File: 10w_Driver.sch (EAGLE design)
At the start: 24 parts, among them IC1 78L05Z, T4 2N3904, T5 22-23-2021, T6 22-23-2041, T7 2N3904, T8 2N3904, U1 PT4115PT4115B89E, U2 PT4115PT4115B89E, U3 PT4115PT4115B89E

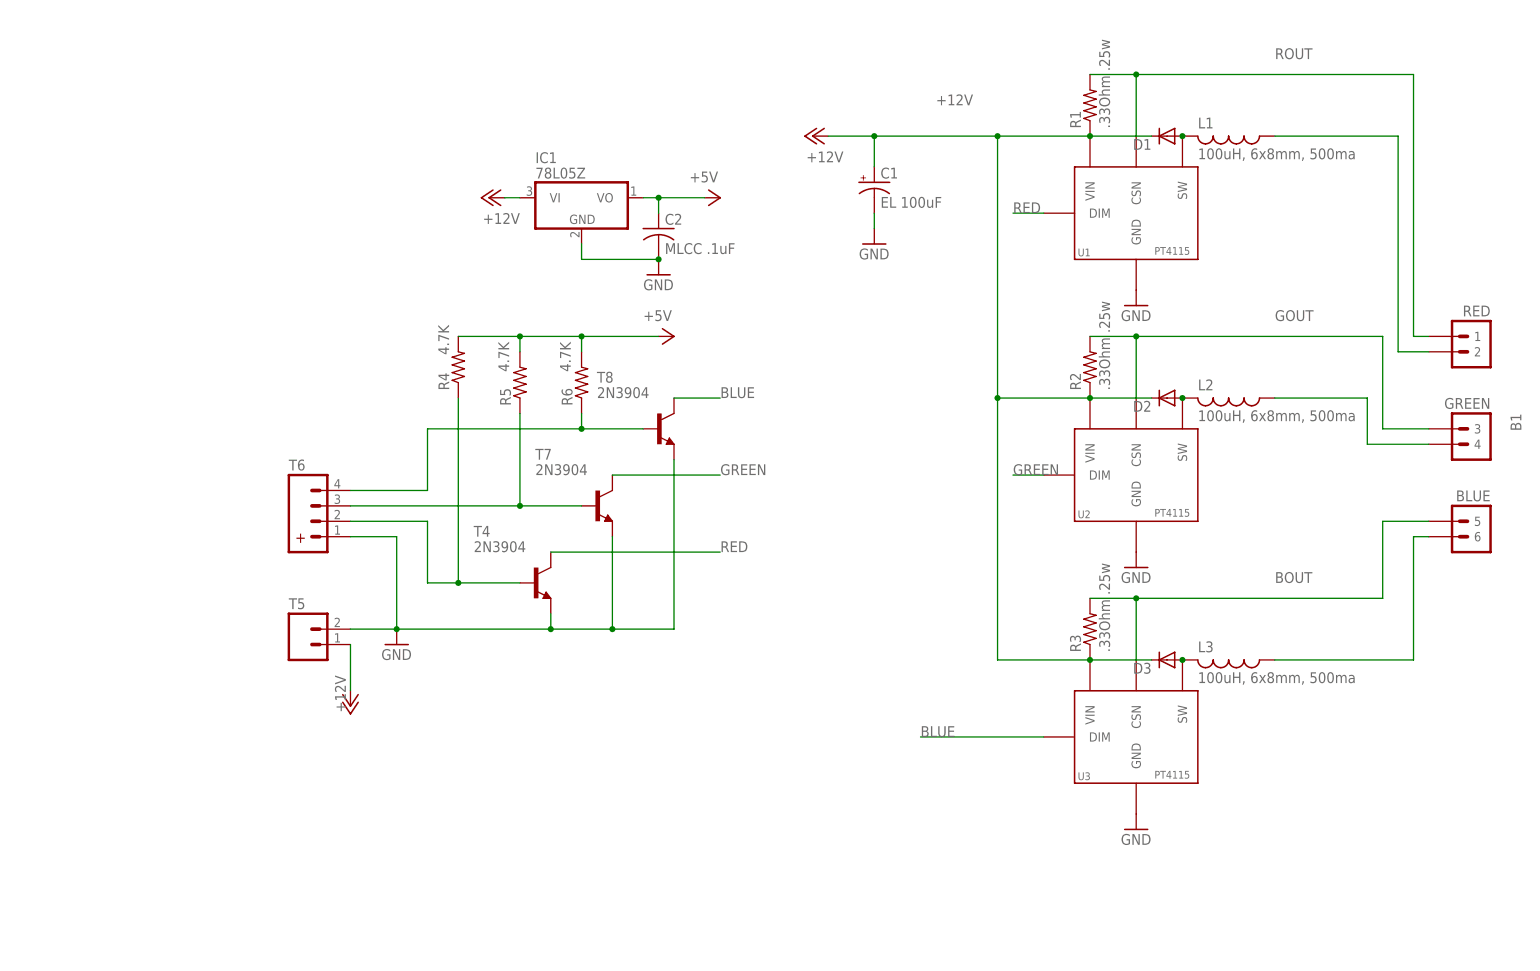
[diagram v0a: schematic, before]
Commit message: Initial Design with ws2811
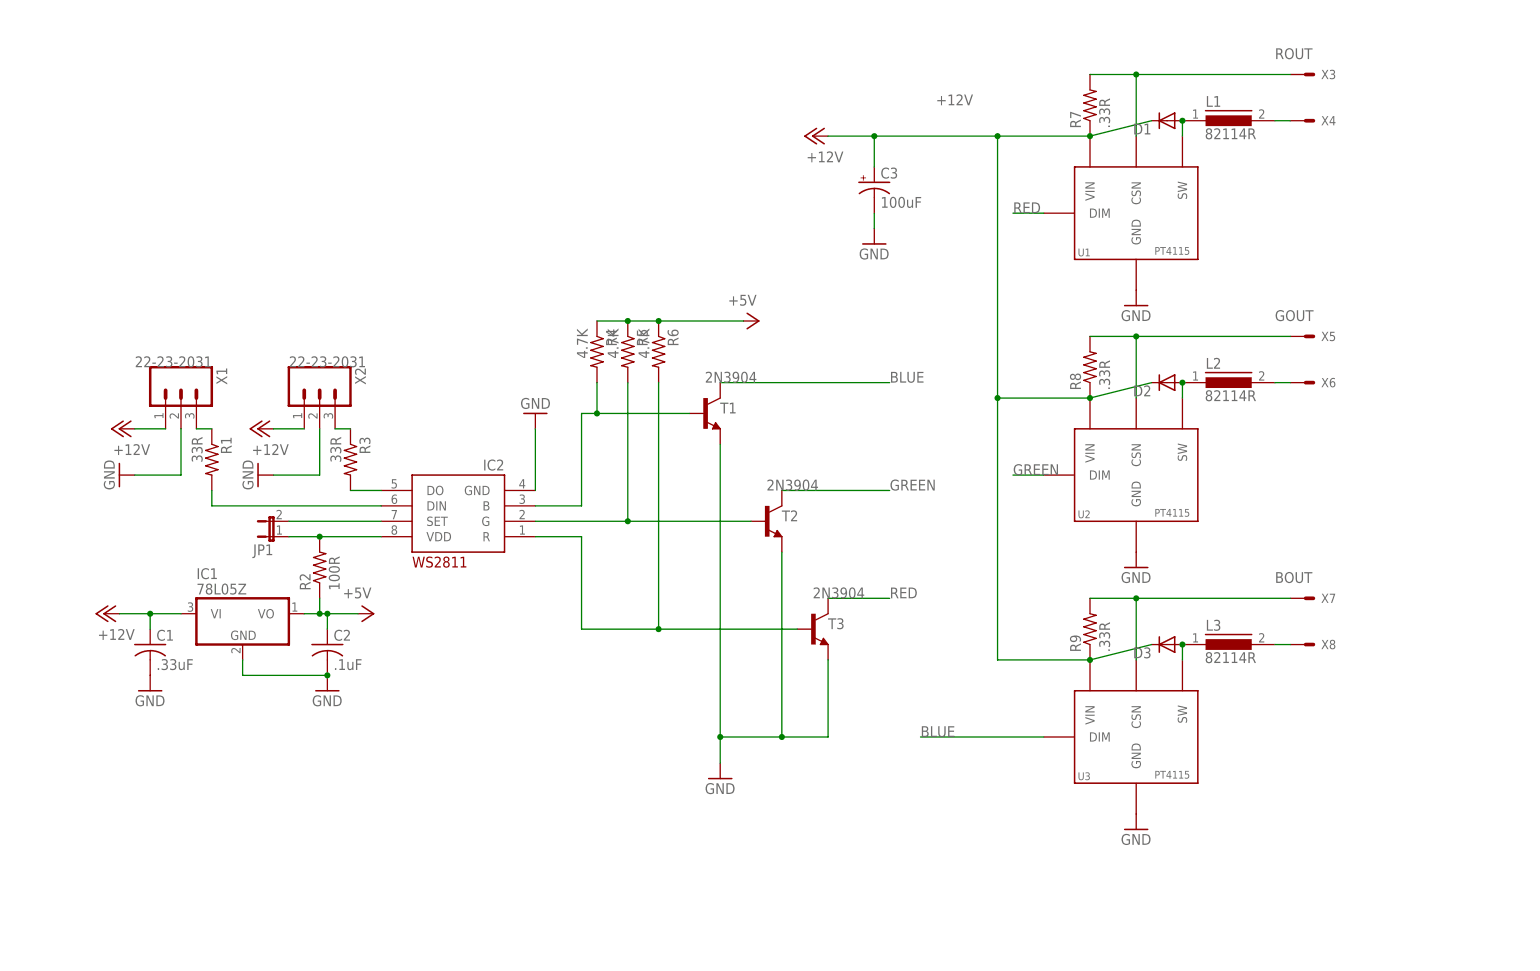
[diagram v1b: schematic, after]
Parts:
- removed B1: LED-BOARD, MyLibrary:LED-BOARD
- removed T4, T7, T8: 2N3904, transistor:2N3904
- removed T5: 22-23-2021, MyLibrary:22-23-2021
- removed T6: 22-23-2041, MyLibrary:22-23-2041
- added C3: 100uF, rcl:CPOL-USTT2D6L
- added IC2: WS2811-SOP8, MyLibrary:WS2811-SOP8
- added JP1: (no value), jumper:JP1E
- added R7, R8, R9: .33R, resistor:R-US_0204/5
- added T1, T2, T3: 2N3904, transistor:2N3904
- added X1, X2: 22-23-2031, MyLibrary:22-23-2031
- added X3, X4, X5, X6, X7, X8: LED-PAD, MyLibrary:LED-PAD
- C1: value EL 100uF -> .33uF; device rcl:CPOL-USTT2D6L -> rcl:C-US025-025X050
- C2: value MLCC .1uF -> .1uF; device rcl:C-US050-030X075 -> rcl:C-US025-025X050
- L1, L2, L3: value 100uH, 6x8mm, 500ma -> 82114R; device MyLibrary:INDUCTOR -> inductors:82114R
- R1, R3: value .33Ohm .25w -> 33R; device resistor:R-US_0204/5 -> rcl:R-US_0204/5
- R2: value .33Ohm .25w -> 100R; device resistor:R-US_0204/5 -> rcl:R-US_0204/5
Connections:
- new net N$16: IC2.SET, JP1.2
- new net N$18: IC2.G, R5.2, T2.B
- new net N$20: IC2.R, R6.2, T3.B
- new net N$7: IC2.DO, R3.2
- new net N$8: IC2.DIN, R1.2
- new net N$9: L2.2, X6.S
- net +12V: now also C1.1, C3.+, R7.1, R8.1, R9.1, X1.1, X2.1; no longer C1.+, R1.1, R2.1, R3.1, T5.1
- net +5V: now also R2.1, R4.1, R5.1, R6.1; no longer R4.2, R5.2, R6.2
- net BLUE: now also T1.C; no longer T8.C
- net BOUT: now also R9.2, X7.S; no longer B1.5, R3.2
- net GND: now also C1.2, C3.-, IC2.GND, T1.E, T2.E, T3.E, X1.2, X2.2; no longer C1.-, T4.E, T5.2, T6.1, T7.E, T8.E
- net GOUT: now also R8.2, X5.S; no longer B1.3, R2.2
- net GREEN: now also T2.C; no longer T7.C
- net N$1: now also L1.1; no longer L1.2
- net N$10: now also L3.2, X8.S; no longer R4.1, T4.B, T6.2
- net N$14: now also IC2.VDD, JP1.1, R2.2; no longer R5.1, T6.3, T7.B
- net N$15: now also IC2.B, R4.2, T1.B; no longer R6.1, T6.4, T8.B
- net N$2: now also L3.1; no longer L3.2
- net N$3: now also L1.2, X4.S; no longer B1.2, L1.1
- net N$4: now also R3.1, X2.3; no longer B1.4, L2.1
- net N$5: now also L2.1; no longer L2.2
- net N$6: now also R1.1, X1.3; no longer B1.6, L3.1
- net RED: now also T3.C; no longer T4.C
- net ROUT: now also R7.2, X3.S; no longer B1.1, R1.2
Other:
- moved on the sheet: C2, D1, D2, D3, IC1, R1, R2, R3, R4, R5, R6

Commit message: Final 1.1
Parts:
- R2: value 100R -> 100ohm
- R4, R5, R6: value 4.7K -> 4.7k
- R7, R8, R9: value .33R -> .33
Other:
- moved on the sheet: C3, D1, D3, L1, L3, R7, R8, U1, U3, X3, X4, X5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

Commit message: Final 1.1 with Inverter
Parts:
- removed C3: 100uF, rcl:CPOL-USTT2D6L
- removed R7, R8, R9: .33, resistor:R-US_0204/5
- removed T1, T2, T3: 2N3904, transistor:2N3904
- added IC3: TC7W04FTC7W04F, MyLibrary:TC7W04FTC7W04F
- added TP1: TPB2,54, testpad:TPB2,54
- added TP2: PTR1TP20SQ, testpad:PTR1TP20SQ
- C1: value .33uF -> EL 100uF; device rcl:C-US025-025X050 -> rcl:CPOL-USTT2D6L
- C2: device rcl:C-US025-025X050 -> resistor:CPOL-USB45181A
- JP1: device jumper:JP1E -> jumper:JP2E
- L1, L2, L3: value 82114R -> SLF7045; device inductors:82114R -> inductors:SLF7045
- R1: value 33R -> .3ohm .25w; device rcl:R-US_0204/5 -> resistor:R-US_R0805
- R2: value 100ohm -> 33R; device rcl:R-US_0204/5 -> rcl:R-US_M0805
- R3: device rcl:R-US_0204/5 -> rcl:R-US_M0805
- R4: value 4.7k -> 100ohm; device resistor:R-US_0204/5 -> rcl:R-US_M0805
- R5: value 4.7k -> .3hm .25w; device resistor:R-US_0204/5 -> resistor:R-US_M0805
- R6: value 4.7k -> .3ohm .25w; device resistor:R-US_0204/5 -> resistor:R-US_R0805
- U1, U2, U3: device MyLibrary:PT4115PT4115B89E -> IC:PT4115PT4115B89E
- X2: value 22-23-2031 -> LED-PAD; device MyLibrary:22-23-2031 -> MyLibrary:LED-PAD
- X4: value LED-PAD -> 22-23-2031; device MyLibrary:LED-PAD -> MyLibrary:22-23-2031
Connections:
- removed net N$20: IC2.R, R6.2, T3.B
- new net N$19: IC2.G, IC3G$3.I
- net +12V: now also C1.+, R1.2, R5.2, R6.2, X4.1; no longer C1.1, C3.+, R7.1, R8.1, R9.1, X2.1
- net +5V: now also C2.+, IC3VCC.S, TP1.TP; no longer C2.1, R2.1, R5.1, R6.1
- net BLUE: now also IC3G$1.O; no longer T1.C
- net BOUT: now also R6.1; no longer R9.2
- net GND: now also C1.-, C2.-, IC3GND.S, TP2.TP, X4.2; no longer C1.2, C2.2, C3.-, T1.E, T2.E, T3.E, X2.2
- net GOUT: now also R5.1; no longer R8.2
- net GREEN: now also IC3G$3.O; no longer T2.C
- net N$14: now also JP1.2, R4.2; no longer JP1.1, R2.2
- net N$15: now also IC2.R, IC3G$2.I; no longer IC2.B, R4.2, T1.B
- net N$16: now also IC2.B, IC3G$1.I; no longer IC2.SET, JP1.2
- net N$18: now also IC2.SET, JP1.3; no longer IC2.G, R5.2, T2.B
- net N$3: now also X3.S; no longer X4.S
- net N$4: now also X4.3; no longer X2.3
- net N$6: now also R2.1; no longer R1.1
- net N$8: now also R2.2; no longer R1.2
- net RED: now also IC3G$2.O; no longer T3.C
- net ROUT: now also R1.1, X2.S; no longer R7.2, X3.S
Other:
- moved on the sheet: D1, D2, D3, IC1, IC2, R1, R2, R3, R4, R5, R6, U1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

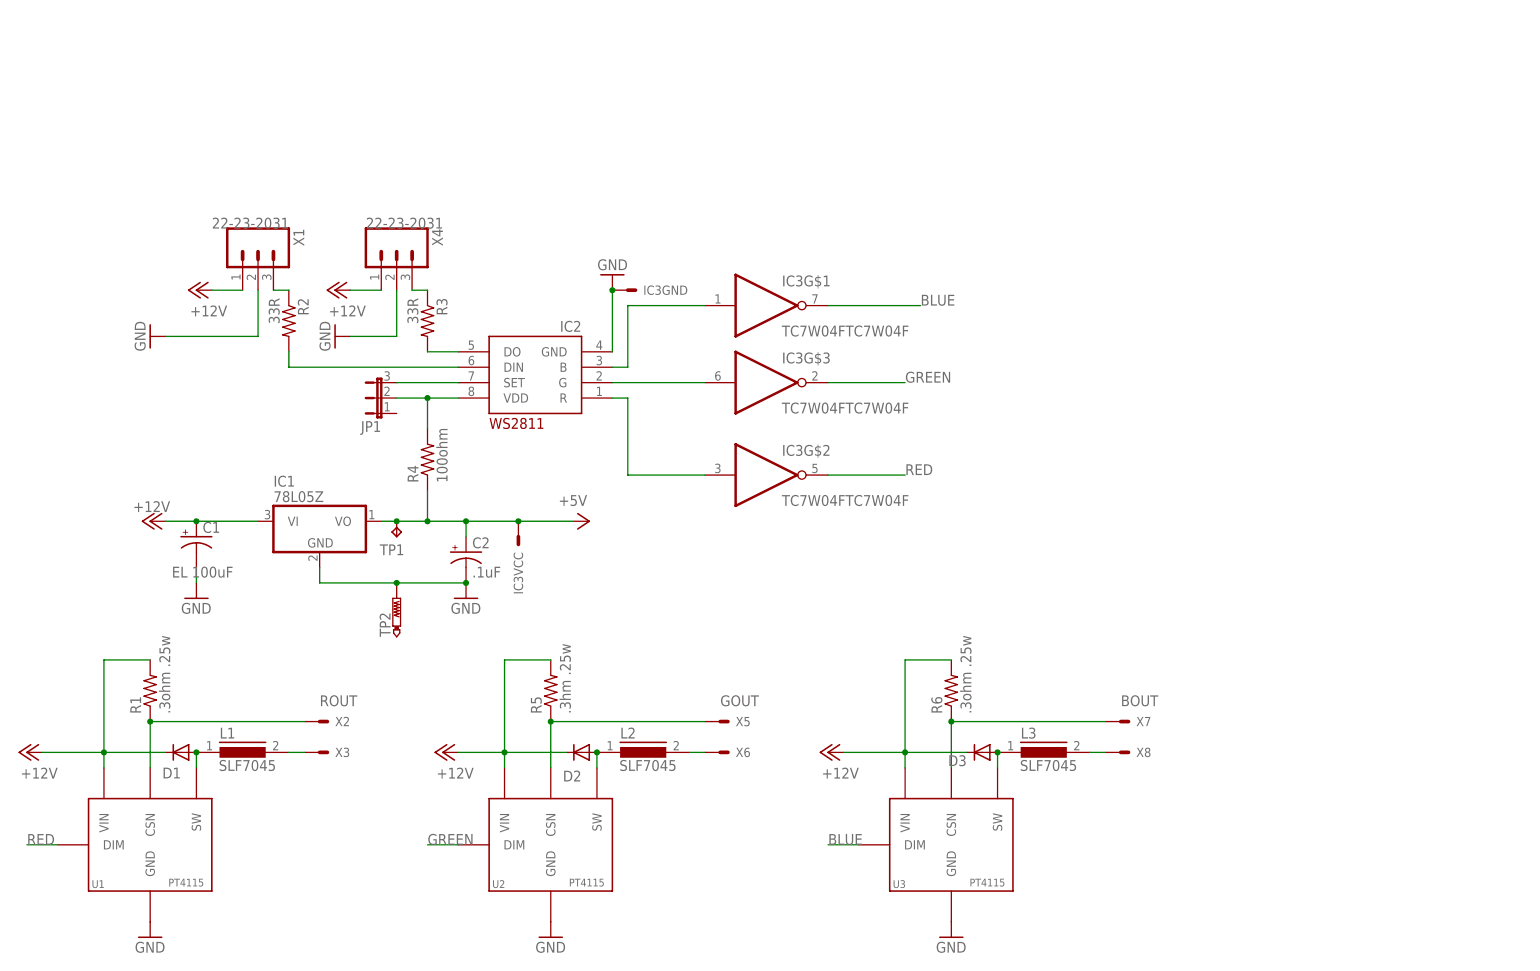
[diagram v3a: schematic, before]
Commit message: Reworked Inverter Layout
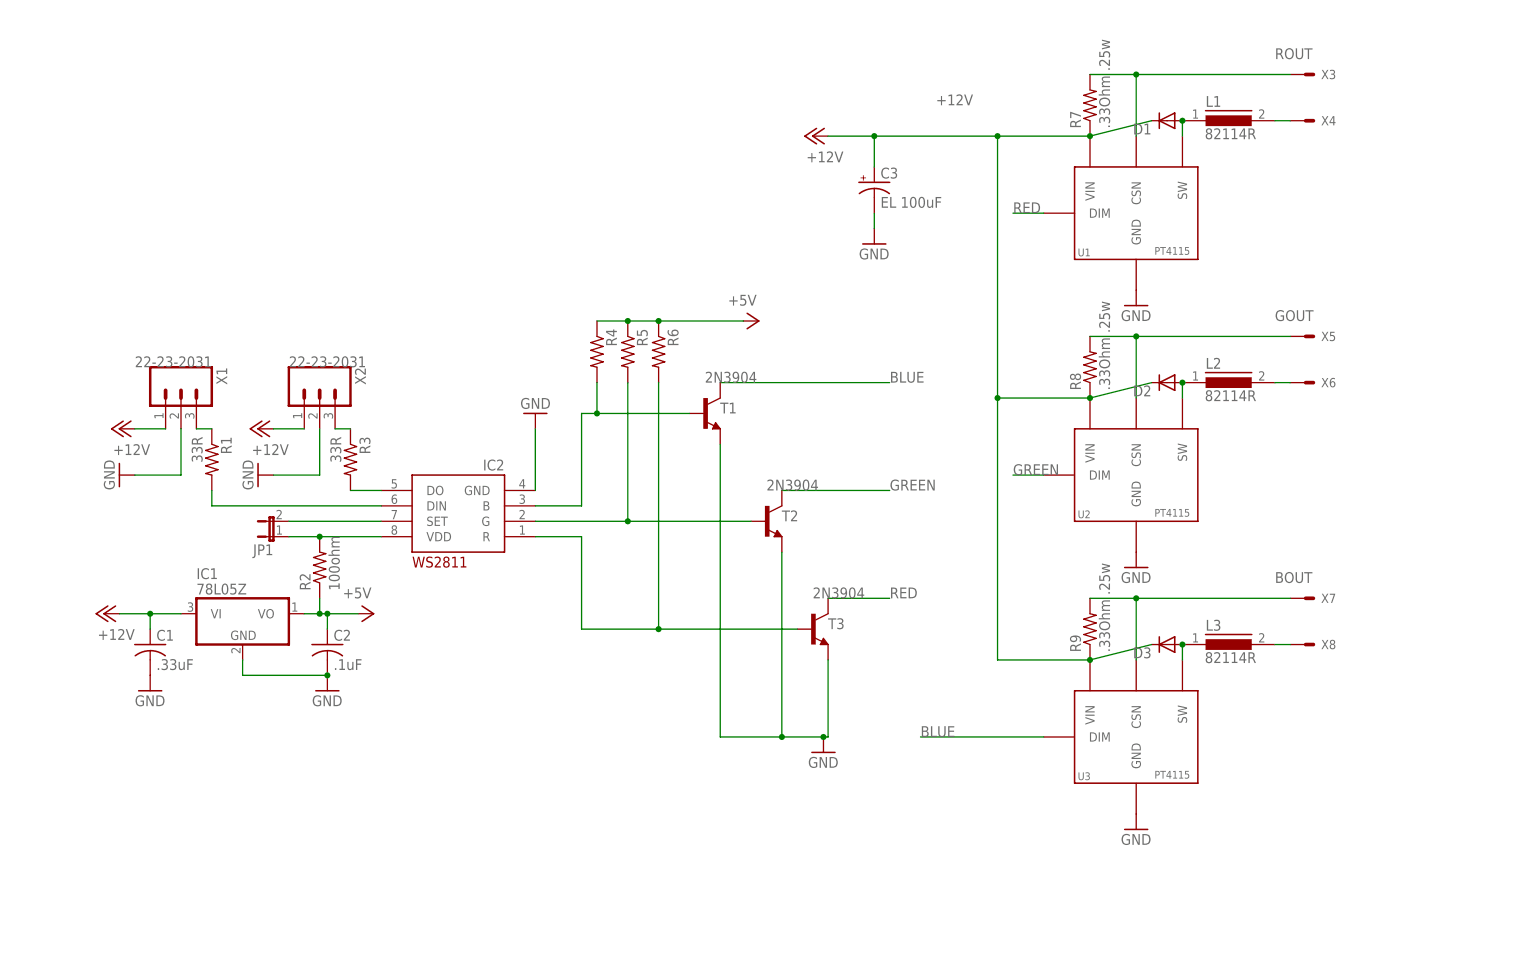
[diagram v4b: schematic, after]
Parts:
- removed IC3: TC7W04FTC7W04F, MyLibrary:TC7W04FTC7W04F
- removed TP1: TPB2,54, testpad:TPB2,54
- removed TP2: PTR1TP20SQ, testpad:PTR1TP20SQ
- added C3: EL 100uF, rcl:CPOL-USTT2D6L
- added R7, R8, R9: .33Ohm .25w, resistor:R-US_0204/5
- added T1, T2, T3: 2N3904, transistor:2N3904
- C1: value EL 100uF -> .33uF; device rcl:CPOL-USTT2D6L -> rcl:C-US025-025X050
- C2: device resistor:CPOL-USB45181A -> rcl:C-US025-025X050
- JP1: device jumper:JP2E -> jumper:JP1E
- L1, L2, L3: value SLF7045 -> 82114R; device inductors:SLF7045 -> inductors:82114R
- R1: value .3ohm .25w -> 33R; device resistor:R-US_R0805 -> rcl:R-US_0204/5
- R2: value 33R -> 100ohm; device rcl:R-US_M0805 -> rcl:R-US_0204/5
- R3: device rcl:R-US_M0805 -> rcl:R-US_0204/5
- R4: value 100ohm -> (none); device rcl:R-US_M0805 -> resistor:R-US_0204/5
- R5: value .3hm .25w -> (none); device resistor:R-US_M0805 -> resistor:R-US_0204/5
- R6: value .3ohm .25w -> (none); device resistor:R-US_R0805 -> resistor:R-US_0204/5
- U1, U2, U3: device IC:PT4115PT4115B89E -> MyLibrary:PT4115PT4115B89E
- X2: value LED-PAD -> 22-23-2031; device MyLibrary:LED-PAD -> MyLibrary:22-23-2031
- X4: value 22-23-2031 -> LED-PAD; device MyLibrary:22-23-2031 -> MyLibrary:LED-PAD
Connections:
- removed net N$19: IC2.G, IC3G$3.I
- new net N$20: IC2.R, R6.2, T3.B
- net +12V: now also C1.1, C3.+, R7.1, R8.1, R9.1, X2.1; no longer C1.+, R1.2, R5.2, R6.2, X4.1
- net +5V: now also C2.1, R2.1, R5.1, R6.1; no longer C2.+, IC3VCC.S, TP1.TP
- net BLUE: now also T1.C; no longer IC3G$1.O
- net BOUT: now also R9.2; no longer R6.1
- net GND: now also C1.2, C2.2, C3.-, T1.E, T2.E, T3.E, X2.2; no longer C1.-, C2.-, IC3GND.S, TP2.TP, X4.2
- net GOUT: now also R8.2; no longer R5.1
- net GREEN: now also T2.C; no longer IC3G$3.O
- net N$14: now also JP1.1, R2.2; no longer JP1.2, R4.2
- net N$15: now also IC2.B, R4.2, T1.B; no longer IC2.R, IC3G$2.I
- net N$16: now also IC2.SET, JP1.2; no longer IC2.B, IC3G$1.I
- net N$18: now also IC2.G, R5.2, T2.B; no longer IC2.SET, JP1.3
- net N$3: now also X4.S; no longer X3.S
- net N$4: now also X2.3; no longer X4.3
- net N$6: now also R1.1; no longer R2.1
- net N$8: now also R1.2; no longer R2.2
- net RED: now also T3.C; no longer IC3G$2.O
- net ROUT: now also R7.2, X3.S; no longer R1.1, X2.S
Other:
- moved on the sheet: D1, D2, D3, IC1, IC2, R1, R2, R3, R4, R5, R6, U1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

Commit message: Reworked Layout
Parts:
- removed C3: EL 100uF, rcl:CPOL-USTT2D6L
- removed R7, R8, R9: .33Ohm .25w, resistor:R-US_0204/5
- removed T1, T2, T3: 2N3904, transistor:2N3904
- added IC3: TC7W04FTC7W04F, MyLibrary:TC7W04FTC7W04F
- added TP1: TPB2,54, testpad:TPB2,54
- added TP2: PTR1TP20SQ, testpad:PTR1TP20SQ
- C1: value .33uF -> EL 100uF; device rcl:C-US025-025X050 -> rcl:CPOL-USTT2D6L
- C2: device rcl:C-US025-025X050 -> resistor:CPOL-USB45181A
- JP1: device jumper:JP1E -> jumper:JP2E
- L1, L2, L3: value 82114R -> SLF7045; device inductors:82114R -> inductors:SLF7045
- R1: value 33R -> .3ohm .25w; device rcl:R-US_0204/5 -> resistor:R-US_R1206
- R2: value 100ohm -> 33R; device rcl:R-US_0204/5 -> rcl:R-US_M0805
- R3: device rcl:R-US_0204/5 -> rcl:R-US_M0805
- R4: value (none) -> 100ohm; device resistor:R-US_0204/5 -> rcl:R-US_M0805
- R5: value (none) -> .3hm .25w; device resistor:R-US_0204/5 -> resistor:R-US_M1206
- R6: value (none) -> .3ohm .25w; device resistor:R-US_0204/5 -> resistor:R-US_R1206
- U1, U2, U3: device MyLibrary:PT4115PT4115B89E -> IC:PT4115PT4115B89E
- X2: value 22-23-2031 -> LED-PAD; device MyLibrary:22-23-2031 -> MyLibrary:LED-PAD
- X4: value LED-PAD -> 22-23-2031; device MyLibrary:LED-PAD -> MyLibrary:22-23-2031
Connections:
- removed net N$20: IC2.R, R6.2, T3.B
- new net N$19: IC2.G, IC3G$3.I
- net +12V: now also C1.+, R1.2, R5.2, R6.2, X4.1; no longer C1.1, C3.+, R7.1, R8.1, R9.1, X2.1
- net +5V: now also C2.+, IC3VCC.S, TP1.TP; no longer C2.1, R2.1, R5.1, R6.1
- net BLUE: now also IC3G$1.O; no longer T1.C
- net BOUT: now also R6.1; no longer R9.2
- net GND: now also C1.-, C2.-, IC3GND.S, TP2.TP, X4.2; no longer C1.2, C2.2, C3.-, T1.E, T2.E, T3.E, X2.2
- net GOUT: now also R5.1; no longer R8.2
- net GREEN: now also IC3G$3.O; no longer T2.C
- net N$14: now also JP1.2, R4.2; no longer JP1.1, R2.2
- net N$15: now also IC2.R, IC3G$2.I; no longer IC2.B, R4.2, T1.B
- net N$16: now also IC2.B, IC3G$1.I; no longer IC2.SET, JP1.2
- net N$18: now also IC2.SET, JP1.3; no longer IC2.G, R5.2, T2.B
- net N$3: now also X3.S; no longer X4.S
- net N$4: now also X4.3; no longer X2.3
- net N$6: now also R2.1; no longer R1.1
- net N$8: now also R2.2; no longer R1.2
- net RED: now also IC3G$2.O; no longer T3.C
- net ROUT: now also R1.1, X2.S; no longer R7.2, X3.S
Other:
- moved on the sheet: D1, D2, D3, IC1, IC2, R1, R2, R3, R4, R5, R6, U1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
